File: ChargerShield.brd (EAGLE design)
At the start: 68.6 x 53.3 mm, 23 parts, among them Q1 BD648, T2 BC548, X1 +5V, X2 Battery, X3 VCC

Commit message: added software and board
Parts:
- R5: device rcl:0207/10 -> rcl:0207/15
- moved X1 40.6 mm to (5.08, 10.2), turned to 90 degrees
- moved D3 34.5 mm to (12.7, 20.3), turned to 90 degrees
- moved R5 18.0 mm to (48.3, 20.3), turned to 270 degrees
- moved R1 9.16 mm to (20.3, 45.7), turned to 0 degrees
- moved LED1 8.98 mm to (12.7, 41.9), turned to 270 degrees
- moved X3 2.54 mm to (5.08, 22.9)
- moved D1 2.54 mm to (55.9, 22.9)
- moved JP1 2.54 mm to (16.5, 35.6)
- moved R4 2.54 mm to (35.6, 43.2)
- moved R6 2.54 mm to (50.8, 17.8)
- moved R7 2.54 mm to (26.7, 30.5)
- moved L1 1.27 mm to (43.2, 22.9)
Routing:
- net GND: track 0.00 -> 94.0 mm
- net N$12: track 0.00 -> 61.2 mm
- net U_BATT: track 0.00 -> 54.6 mm
- net VCC: track 0.00 -> 49.5 mm
- net N$13: track 0.00 -> 44.0 mm
- net +5V: track 0.00 -> 36.9 mm, vias 0 -> 2
- net N$6: track 0.00 -> 25.7 mm
- net N$9: track 0.00 -> 20.3 mm
- net N$7: track 0.00 -> 14.0 mm
- net N$10: track 0.00 -> 14.0 mm
- net N$11: track 0.00 -> 12.7 mm
- net PWM: track 0.00 -> 8.17 mm
- net N$1: track 0.00 -> 7.67 mm
- net N$4: track 0.00 -> 7.28 mm
- net N$3: track 0.00 -> 6.97 mm
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- added copper zone on layer 16, net GND

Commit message: update
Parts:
- moved T2 2.54 mm to (30.5, 38.1), turned to 0 degrees
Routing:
- net N$6: track 25.7 -> 30.8 mm
- net GND: track 94.0 -> 96.5 mm
- net N$5: track 5.71 -> 3.17 mm
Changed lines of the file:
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@@
 <element name="S1" library="SparkFun-Electromechanical" package="TACTILE-PTH" value="Down" x="60.96" y="43.18" rot="R270"/>
 <element name="S2" library="SparkFun-Electromechanical" package="TACTILE-PTH" value="UP" x="50.8" y="43.18" rot="R270"/>
-<element name="T2" library="transistor" package="TO92" value="BC548" x="33.02" y="38.1" rot="R90"/>
+<element name="T2" library="transistor" package="TO92" value="BC548" x="30.48" y="38.1"/>
 <element name="R4" library="rcl" package="0207/10" value="2k2" x="35.56" y="43.18" rot="R180"/>
 <element name="R5" library="rcl" package="0207/15" value="1k" x="48.26" y="20.32" rot="R270"/>
@@
 <wire x1="27.94" y1="43.18" x2="27.94" y2="45.72" width="0.8128" layer="16"/>
 <wire x1="27.94" y1="45.72" x2="35.56" y2="45.72" width="0.8128" layer="16"/>
-<wire x1="35.56" y1="45.72" x2="35.56" y2="39.37" width="0.8128" layer="16"/>
-<wire x1="35.56" y1="39.37" x2="33.02" y2="39.37" width="0.8128" layer="16"/>
+<wire x1="35.56" y1="45.72" x2="35.56" y2="38.1" width="0.8128" layer="16"/>
+<wire x1="35.56" y1="38.1" x2="31.75" y2="38.1" width="0.8128" layer="16"/>
 <wire x1="64.77" y1="31.75" x2="83.82" y2="34.671" width="0" layer="19" extent="16-16"/>
 </signal>
@@
 <contactref element="R4" pad="2"/>
 <contactref element="T2" pad="2"/>
-<wire x1="30.48" y1="43.18" x2="30.48" y2="38.1" width="0.6604" layer="16"/>
-<wire x1="30.48" y1="38.1" x2="31.115" y2="38.1" width="0.6604" layer="16"/>
+<wire x1="30.48" y1="43.18" x2="30.48" y2="40.64" width="0.6604" layer="16"/>
+<wire x1="30.48" y1="40.64" x2="30.48" y2="40.005" width="0.6604" layer="16"/>
 </signal>
 <signal name="N$6">
 <contactref element="T2" pad="3"/>
 <contactref element="R5" pad="1"/>
-<wire x1="33.02" y1="36.83" x2="33.02" y2="26.67" width="0.6604" layer="16"/>
-<wire x1="33.02" y1="26.67" x2="45.72" y2="26.67" width="0.6604" layer="16"/>
+<wire x1="29.21" y1="38.1" x2="29.21" y2="26.67" width="0.6604" layer="16"/>
+<wire x1="29.21" y1="26.67" x2="45.72" y2="26.67" width="0.6604" layer="16"/>
 <wire x1="45.72" y1="26.67" x2="48.26" y2="27.94" width="0.6604" layer="16"/>
 </signal>
@@
 <contactref element="R6" pad="1"/>
 <contactref element="Q1" pad="1"/>
-<wire x1="36.83" y1="12.7" x2="48.26" y2="12.7" width="0.6604" layer="16"/>
-<wire x1="48.26" y1="12.7" x2="50.8" y2="12.7" width="0.6604" layer="16"/>
+<wire x1="36.83" y1="12.7" x2="48.26" y2="12.7" width="1.27" layer="16"/>
+<wire x1="48.26" y1="12.7" x2="50.8" y2="12.7" width="1.27" layer="16"/>
 </signal>
 <signal name="VCC">
@@
 <contactref element="Q1" pad="2"/>
 <contactref element="L1" pad="1"/>
-<wire x1="36.83" y1="15.24" x2="43.18" y2="15.24" width="0.6604" layer="16"/>
-<wire x1="43.18" y1="16.51" x2="43.18" y2="15.24" width="0.6604" layer="16"/>
-<wire x1="43.18" y1="15.24" x2="55.88" y2="15.24" width="0.6604" layer="16"/>
+<wire x1="36.83" y1="15.24" x2="43.18" y2="15.24" width="1.27" layer="16"/>
+<wire x1="43.18" y1="16.51" x2="43.18" y2="15.24" width="1.27" layer="16"/>
+<wire x1="43.18" y1="15.24" x2="55.88" y2="15.24" width="1.27" layer="16"/>
 </signal>
 <signal name="N$10">
@@
 <wire x1="29.21" y1="22.86" x2="27.94" y2="22.86" width="0.6604" layer="16"/>
 <wire x1="26.67" y1="24.13" x2="25.4" y2="22.86" width="0.6604" layer="16"/>
-<wire x1="59.69" y1="26.67" x2="64.77" y2="21.59" width="0.6604" layer="16"/>
+<wire x1="59.69" y1="26.67" x2="64.77" y2="21.59" width="1.27" layer="16"/>
 <wire x1="49.53" y1="26.67" x2="59.69" y2="26.67" width="0.6604" layer="16"/>
 <wire x1="46.99" y1="25.4" x2="49.53" y2="26.67" width="0.6604" layer="16"/>
@@
 <contactref element="R8" pad="1"/>
 <contactref element="X2" pad="1"/>
-<wire x1="64.77" y1="16.51" x2="64.77" y2="10.16" width="0.6604" layer="16"/>
+<wire x1="64.77" y1="16.51" x2="64.77" y2="10.16" width="1.27" layer="16"/>
 <wire x1="33.02" y1="24.13" x2="31.75" y2="22.86" width="0.6604" layer="16"/>
 <wire x1="48.26" y1="24.13" x2="33.02" y2="24.13" width="0.6604" layer="16"/>

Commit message: current sense
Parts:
- added IC1: LM324N, linear:DIL14
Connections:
- new net V+: IC1.4
- new net V-: IC1.11
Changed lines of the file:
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@@
 <attribute name="OC_FARNELL" value="unknown" x="-7.62" y="10.16" size="1.778" layer="27" rot="R90" display="off"/>
 </element>
+<element name="IC1" library="linear" package="DIL14" value="LM324N" x="5.08" y="-7.62"/>
 </elements>
 <signals>
@@
 <wire x1="64.77" y1="16.51" x2="64.77" y2="16.63" width="0.6604" layer="16"/>
 </signal>
+<signal name="V+">
+<contactref element="IC1" pad="4"/>
+</signal>
+<signal name="V-">
+<contactref element="IC1" pad="11"/>
+</signal>
 </signals>

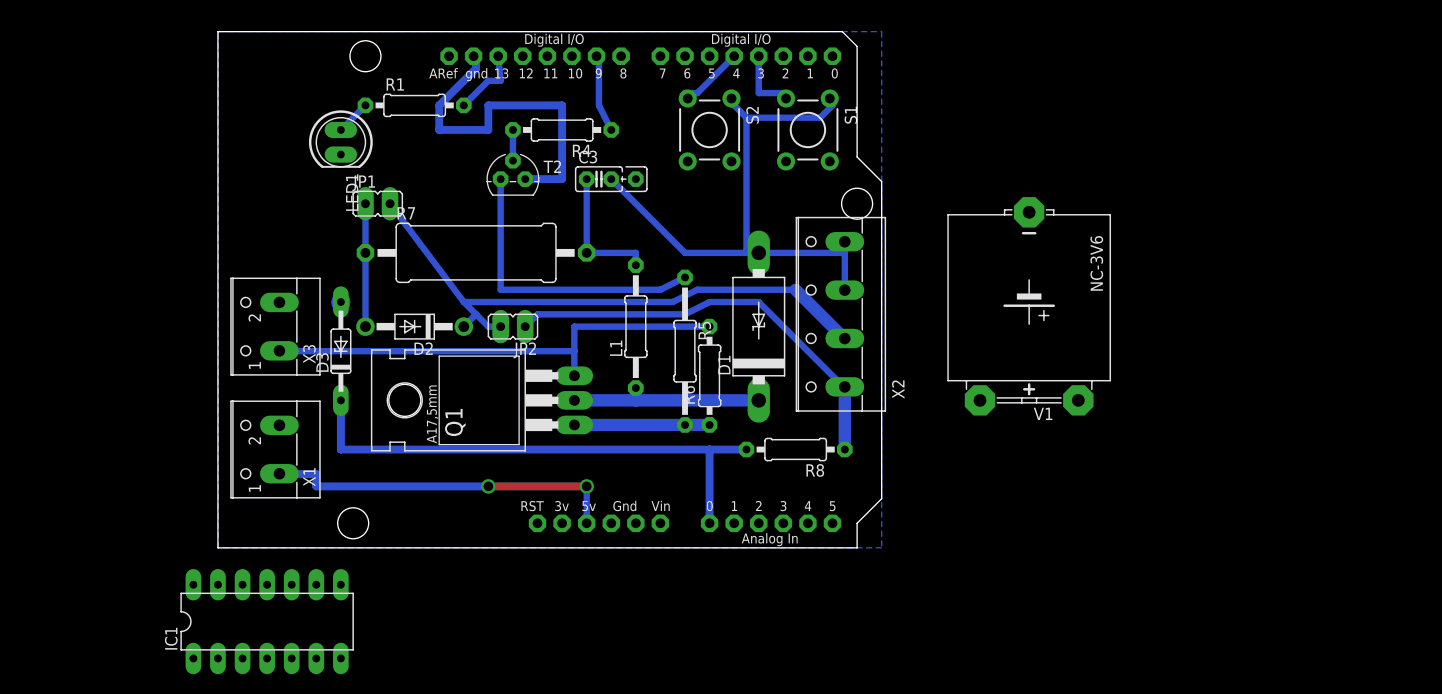
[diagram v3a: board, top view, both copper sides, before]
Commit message: start button and current sense program
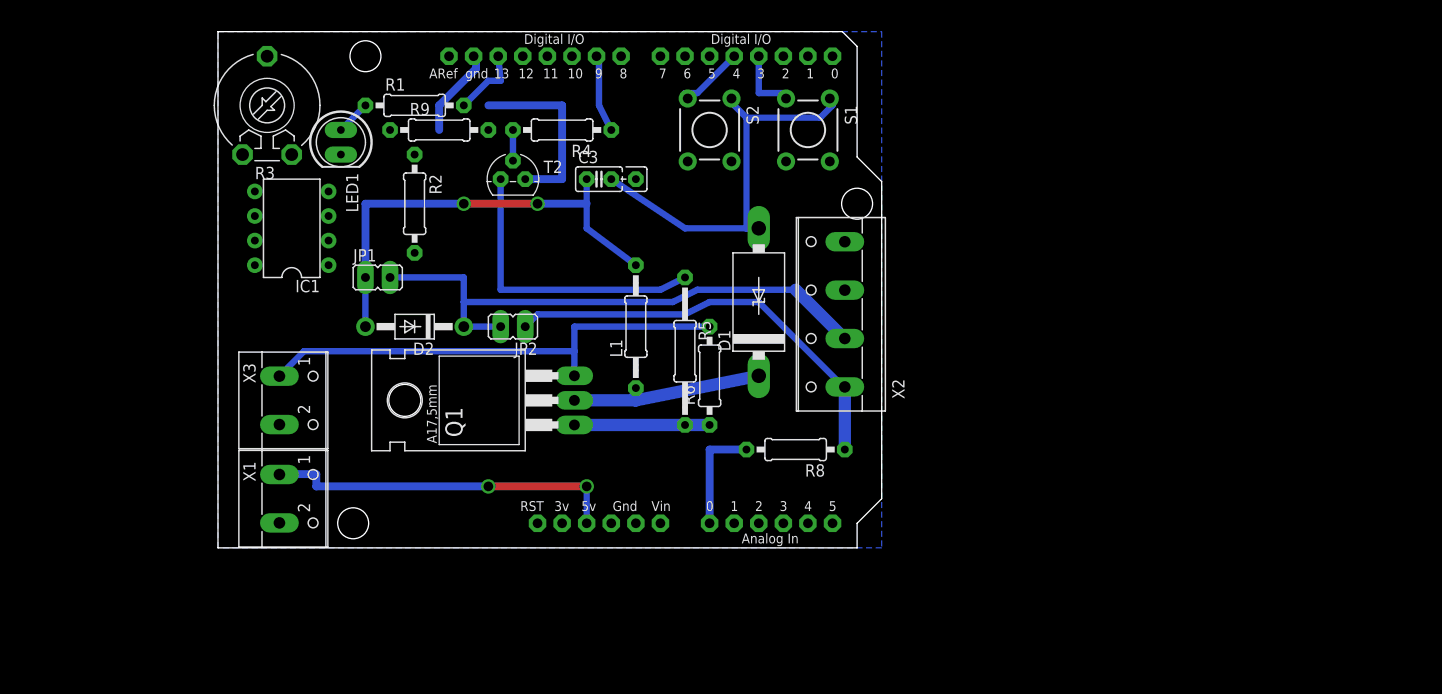
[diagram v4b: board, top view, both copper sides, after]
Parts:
- removed D3: 5V1, diode:DO35Z10
- removed R7: 1, rcl:0617/22
- removed V1: BATTERY, Misc:3V60R
- added R2: 100k, rcl:0207/10
- added R3: (no value), pot:LI10
- added R9: 1k, rcl:0207/10
- IC1: value LM324N -> LM358N; device linear:DIL14 -> linear:DIL08
- moved IC1 40.7 mm to (7.62, 33.0), turned to 90 degrees
- moved X3 8.03 mm to (7.62, 15.2), turned to 270 degrees
- moved JP1 7.62 mm to (16.5, 27.9)
- moved X1 5.68 mm to (7.62, 5.08), turned to 270 degrees
- moved D1 2.54 mm to (55.9, 25.4)
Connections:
- removed net N$12: D2.C, JP1.2, JP2.2, V1.+, V1.+@1, X2.2
- new net I_SENSE: IC1.3, X2.4
- new net N$13: D2.C, JP1.2, JP2.2, X2.2
- new net N$14: IC1.2, R2.1, R9.2
- new net N$15: R3.E, R3.S, R9.1
- net GND: now also R3.A; no longer D3.A, V1.-, X2.4
- net N$10: now also D2.A, JP1.1; no longer R7.2
- net N$11: now also IC1.1, R2.2; no longer D2.A, JP1.1, R7.1
- net U_BATT: no longer D3.C
- net V+: now also IC1.8; no longer IC1.4
- net V-: now also IC1.4; no longer IC1.11
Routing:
- net N$12: track 61.2 -> 0.00 mm
- net N$13: track 0.00 -> 58.3 mm
- net U_BATT: track 54.6 -> 11.4 mm
- net N$10: track 14.0 -> 47.0 mm, vias 0 -> 2
- net GND: track 96.5 -> 70.7 mm
- net N$11: track 12.7 -> 0.00 mm
- net VCC: track 49.5 -> 50.6 mm

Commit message: smaller diode
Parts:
- D1: device diode:C4111-15 -> diode:DO35-7
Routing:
- net GND: track 70.7 -> 74.4 mm
- net N$9: track 20.6 -> 21.8 mm
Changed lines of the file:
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@@
 <element name="R6" library="rcl" package="0207/10" value="1k" x="50.8" y="17.78" rot="R90"/>
 <element name="Q1" library="transistor-pnp" package="TO220" value="BD648" x="30.48" y="15.24" rot="R90"/>
-<element name="D1" library="diode" package="C4111-15" value="" x="55.88" y="25.4" rot="R90"/>
+<element name="D1" library="diode" package="DO35-7" value="" x="55.88" y="25.4" rot="R90"/>
 <element name="L1" library="rcl" package="0207/12" value="100µ" x="43.18" y="22.86" rot="R90"/>
 <element name="D2" library="diode" package="DO41-10" value="1N4004" x="20.32" y="22.86" rot="R180"/>
@@
 <wire x1="63.5" y1="45.72" x2="62.23" y2="44.45" width="0.6604" layer="16"/>
 <wire x1="63.5" y1="45.72" x2="63.2206" y2="46.4312" width="0.6604" layer="16"/>
-<wire x1="54.61" y1="33.02" x2="55.88" y2="33.02" width="0.6604" layer="16"/>
+<wire x1="54.61" y1="33.02" x2="55.88" y2="29.21" width="0.6604" layer="16"/>
 <wire x1="48.26" y1="33.02" x2="40.64" y2="38.1" width="0.6604" layer="16"/>
-<wire x1="55.88" y1="33.02" x2="48.26" y2="33.02" width="0.6604" layer="16"/>
+<wire x1="55.88" y1="29.21" x2="48.26" y2="33.02" width="0.6604" layer="16"/>
 <wire x1="54.61" y1="33.02" x2="54.61" y2="44.45" width="0.6604" layer="16"/>
 <wire x1="53.34" y1="45.72" x2="53.0606" y2="46.4312" width="0.6604" layer="16"/>
@@
 <wire x1="36.83" y1="15.24" x2="43.18" y2="15.24" width="1.27" layer="16"/>
 <wire x1="43.18" y1="16.51" x2="43.18" y2="15.24" width="1.27" layer="16"/>
-<wire x1="43.18" y1="15.24" x2="55.88" y2="17.78" width="1.27" layer="16"/>
+<wire x1="43.18" y1="15.24" x2="55.88" y2="21.59" width="1.27" layer="16"/>
 </signal>
 <signal name="N$10">

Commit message: Discharge
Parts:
- added Q2: BD648, transistor-pnp:TO220
- added R7: 1, rcl:0414/15
- R3: value (none) -> 10k
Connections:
- new net N$12: Q2.2, R7.2
- net GND: now also R7.1
- net N$13: now also Q2.3
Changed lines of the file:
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@@
 <element name="IC1" library="linear" package="DIL08" value="LM358N" x="7.62" y="33.02" rot="R90"/>
 <element name="R2" library="rcl" package="0207/10" value="100k" x="20.32" y="35.56" rot="R270"/>
-<element name="R3" library="pot" package="LI10" value="" x="5.08" y="45.72"/>
+<element name="R3" library="pot" package="LI10" value="10k" x="5.08" y="45.72"/>
 <element name="R9" library="rcl" package="0207/10" value="1k" x="22.86" y="43.18"/>
+<element name="R7" library="rcl" package="0414/15" value="1" x="0" y="-5.08"/>
+<element name="Q2" library="transistor-pnp" package="TO220" value="BD648" x="-15.24" y="2.54"/>
 </elements>
 <signals>
@@
 <contactref element="R3" pad="A"/>
 <contactref element="X2" pad="3"/>
+<contactref element="R7" pad="1"/>
+<wire x1="55.88" y1="29.21" x2="64.77" y2="26.63" width="0" layer="19" extent="1-1"/>
+<wire x1="35.56" y1="38.1" x2="40.64" y2="38.1" width="0" layer="19" extent="16-16"/>
+<wire x1="26.67" y1="49.53" x2="27.94" y2="45.72" width="0" layer="19" extent="16-16"/>
+<wire x1="12.7" y1="40.64" x2="22.86" y2="43.18" width="0" layer="19" extent="16-16"/>
+<wire x1="2.54" y1="40.64" x2="12.7" y2="40.64" width="0" layer="19" extent="1-1"/>
+<wire x1="6.35" y1="12.74" x2="2.54" y2="40.64" width="0" layer="19" extent="1-1"/>
+<wire x1="6.35" y1="2.58" x2="6.35" y2="12.74" width="0" layer="19" extent="1-1"/>
+<wire x1="-7.62" y1="-5.08" x2="6.35" y2="2.58" width="0" layer="19" extent="1-1"/>
 </signal>
 <signal name="VIN">
@@
 <wire x1="25.4" y1="25.4" x2="46.99" y2="25.4" width="0.6604" layer="16"/>
 <wire x1="64.77" y1="21.59" x2="64.77" y2="21.63" width="0.6604" layer="16"/>
+<contactref element="Q2" pad="3"/>
+<wire x1="-12.7" y1="-3.81" x2="17.78" y2="27.94" width="0" layer="19" extent="1-1"/>
 </signal>
 <signal name="N$8">
@@
 <wire x1="64.77" y1="16.51" x2="64.77" y2="16.63" width="0.6604" layer="16"/>
 </signal>
+<signal name="N$12">
+<contactref element="Q2" pad="2"/>
+<contactref element="R7" pad="2"/>
+<wire x1="7.62" y1="-5.08" x2="-15.24" y2="-3.81" width="0" layer="19" extent="1-1"/>
+</signal>
 </signals>
